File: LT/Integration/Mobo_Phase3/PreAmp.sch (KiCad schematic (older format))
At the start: 9 parts, among them J8 Conn_01x02_Male, J9 Conn_01x02_Female, Q2 Q_NJFET_DSG

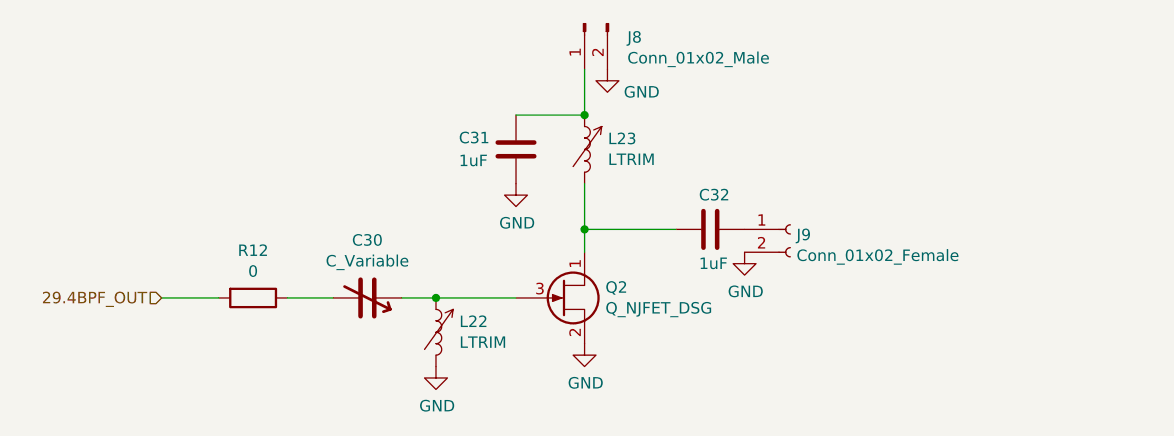
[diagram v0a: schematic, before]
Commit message: Finished PA Schematic Layout with footprints associated with it
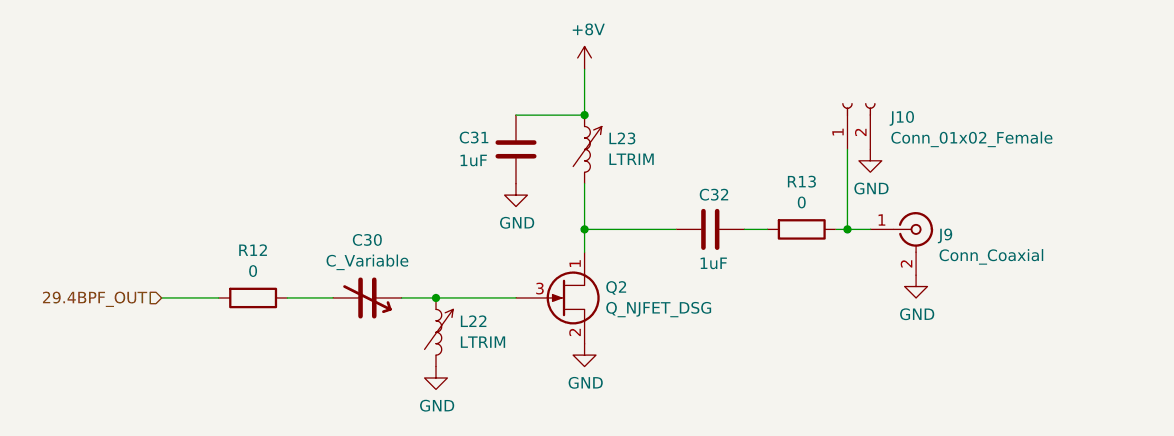
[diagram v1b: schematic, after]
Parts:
- removed J8: Conn_01x02_Male, Connector_PinHeader_2.54mm:PinHeader_1x02_P2.54mm_Vertical, symbol Connector:Conn_01x02_Male
- added J9: Conn_Coaxial, Connector_Coaxial:SMA_Amphenol_132291_Vertical, symbol Connector:Conn_Coaxial
- added R13: 0, Resistor_SMD:R_0805_2012Metric_Pad1.15x1.40mm_HandSolder, symbol Device:R
- renumbered J9 to J10
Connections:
- net GND: now also J9.2 (Ext)
- net +8V: now reaches C31.1, L23.1
- net at C32.1: now also R13.2; no longer J10.1 (Pin_1)
- new net: J10.1 (Pin_1), J9.1 (In), R13.1
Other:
- moved on the sheet: J10
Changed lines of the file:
@@
 	1    0    0    -1
-$EndComp
-$Comp
-L Connector:Conn_01x02_Male J8
-U 1 1 5EB64300
-P 4650 1950
-F 0 "J8" V 4710 1763 50  0000 R CNN
-F 1 "Conn_01x02_Male" V 4801 1763 50  0000 R CNN
-F 2 "Connector_PinHeader_2.54mm:PinHeader_1x02_P2.54mm_Vertical" H 4650 1950 50  0001 C CNN
-F 3 "~" H 4650 1950 50  0001 C CNN
-	1    4650 1950
-	0    -1   1    0
 $EndComp
 Wire Wire Line
 	4650 2150 4650 2350
 Connection ~ 4650 2350
-$Comp
-L power:GND #PWR0107
-U 1 1 5EB64481
-P 4750 2150
-F 0 "#PWR0107" H 4750 1900 50  0001 C CNN
-F 1 "GND" H 4900 2050 50  0000 C CNN
-F 2 "" H 4750 2150 50  0001 C CNN
-F 3 "" H 4750 2150 50  0001 C CNN
-	1    4750 2150
-	1    0    0    -1
-$EndComp
 $Comp
 L Daisy~Chain-cache:Device_C C32
@@
 	4650 2850 4650 2950
 $Comp
-L Connector:Conn_01x02_Female J9
+L Connector:Conn_01x02_Female J10
 U 1 1 5EB64662
-P 5550 2850
-F 0 "J9" H 5577 2826 50  0000 L CNN
-F 1 "Conn_01x02_Female" H 5577 2735 50  0000 L CNN
-F 2 "Connector_PinSocket_2.54mm:PinSocket_1x02_P2.54mm_Vertical" H 5550 2850 50  0001 C CNN
-F 3 "~" H 5550 2850 50  0001 C CNN
-	1    5550 2850
-	1    0    0    -1
+P 5800 2300
+F 0 "J10" V 5740 2112 50  0000 R CNN
+F 1 "Conn_01x02_Female" V 5649 2112 50  0000 R CNN
+F 2 "Connector_PinSocket_2.54mm:PinSocket_1x02_P2.54mm_Vertical" H 5800 2300 50  0001 C CNN
+F 3 "~" H 5800 2300 50  0001 C CNN
+	1    5800 2300
+	0    -1   -1   0
 $EndComp
 $Comp
 L power:GND #PWR0108
 U 1 1 5EB64C4A
-P 5350 2950
-F 0 "#PWR0108" H 5350 2700 50  0001 C CNN
-F 1 "GND" H 5355 2777 50  0000 C CNN
-F 2 "" H 5350 2950 50  0001 C CNN
-F 3 "" H 5350 2950 50  0001 C CNN
-	1    5350 2950
+P 5900 2500
+F 0 "#PWR0108" H 5900 2250 50  0001 C CNN
+F 1 "GND" H 5905 2327 50  0000 C CNN
+F 2 "" H 5900 2500 50  0001 C CNN
+F 3 "" H 5900 2500 50  0001 C CNN
+	1    5900 2500
 	1    0    0    -1
 $EndComp
+$Comp
+L Connector:Conn_Coaxial J9
+U 1 1 5EB6B925
+P 6100 2850
+F 0 "J9" H 6199 2826 50  0000 L CNN
+F 1 "Conn_Coaxial" H 6199 2735 50  0000 L CNN
+F 2 "Connector_Coaxial:SMA_Amphenol_132291_Vertical" H 6100 2850 50  0001 C CNN
+F 3 " ~" H 6100 2850 50  0001 C CNN
+	1    6100 2850
+	1    0    0    -1
+$EndComp
+$Comp
+L power:GND #PWR0109
+U 1 1 5EB6BA87
+P 6100 3050
+F 0 "#PWR0109" H 6100 2800 50  0001 C CNN
+F 1 "GND" H 6105 2877 50  0000 C CNN
+F 2 "" H 6100 3050 50  0001 C CNN
+F 3 "" H 6100 3050 50  0001 C CNN
+	1    6100 3050
+	1    0    0    -1
+$EndComp
+Wire Wire Line
+	5450 2850 5350 2850
+$Comp
+L Device:R R13
+U 1 1 5EB6C81C
+P 5600 2850
+F 0 "R13" V 5393 2850 50  0000 C CNN
+F 1 "0" V 5484 2850 50  0000 C CNN
+F 2 "Resistor_SMD:R_0805_2012Metric_Pad1.15x1.40mm_HandSolder" V 5530 2850 50  0001 C CNN
+F 3 "~" H 5600 2850 50  0001 C CNN
+	1    5600 2850
+	0    1    1    0
+$EndComp
+Wire Wire Line
+	5900 2850 5800 2850
+Wire Wire Line
+	5800 2500 5800 2850
+Connection ~ 5800 2850
+Wire Wire Line
+	5800 2850 5750 2850
+$Comp
+L power:+8V #PWR0107
+U 1 1 5EB725E6
+P 4650 2150
+F 0 "#PWR0107" H 4650 2000 50  0001 C CNN
+F 1 "+8V" H 4665 2323 50  0000 C CNN
+F 2 "" H 4650 2150 50  0001 C CNN
+F 3 "" H 4650 2150 50  0001 C CNN
+	1    4650 2150
+	1    0    0    -1
+$EndComp

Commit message: Changed 2pin headers to 5pin headers for output of pre-amp and input of PA
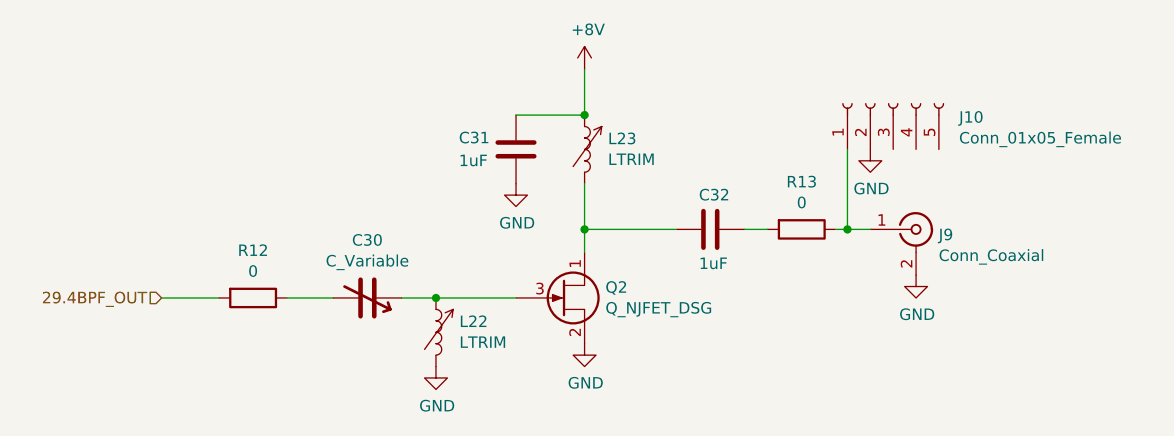
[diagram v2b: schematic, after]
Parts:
- removed J10: Conn_01x02_Female, Connector_PinSocket_2.54mm:PinSocket_1x02_P2.54mm_Vertical, symbol Connector:Conn_01x02_Female
- added J10: Conn_01x05_Female, Connector_PinSocket_2.54mm:PinSocket_1x05_P2.54mm_Vertical, symbol Connector:Conn_01x05_Female
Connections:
- net GND: now also J10.2 (Pin_2)
- net at J9.1 (In), R13.1: now also J10.1 (Pin_1)
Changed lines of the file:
@@
 	4650 2850 4650 2950
-$Comp
-L Connector:Conn_01x02_Female J10
-U 1 1 5EB64662
-P 5800 2300
-F 0 "J10" V 5740 2112 50  0000 R CNN
-F 1 "Conn_01x02_Female" V 5649 2112 50  0000 R CNN
-F 2 "Connector_PinSocket_2.54mm:PinSocket_1x02_P2.54mm_Vertical" H 5800 2300 50  0001 C CNN
-F 3 "~" H 5800 2300 50  0001 C CNN
-	1    5800 2300
-	0    -1   -1   0
-$EndComp
-$Comp
-L power:GND #PWR0108
-U 1 1 5EB64C4A
-P 5900 2500
-F 0 "#PWR0108" H 5900 2250 50  0001 C CNN
-F 1 "GND" H 5905 2327 50  0000 C CNN
-F 2 "" H 5900 2500 50  0001 C CNN
-F 3 "" H 5900 2500 50  0001 C CNN
-	1    5900 2500
-	1    0    0    -1
-$EndComp
 $Comp
 L Connector:Conn_Coaxial J9
@@
 	1    0    0    -1
 $EndComp
+$Comp
+L Connector:Conn_01x05_Female J10
+U 1 1 5EB9C6B4
+P 6000 2300
+F 0 "J10" V 5940 2012 50  0000 R CNN
+F 1 "Conn_01x05_Female" V 5849 2012 50  0000 R CNN
+F 2 "Connector_PinSocket_2.54mm:PinSocket_1x05_P2.54mm_Vertical" H 6000 2300 50  0001 C CNN
+F 3 "~" H 6000 2300 50  0001 C CNN
+	1    6000 2300
+	0    -1   -1   0
+$EndComp
+$Comp
+L power:GND #PWR0108
+U 1 1 5EB9E15B
+P 5900 2500
+F 0 "#PWR0108" H 5900 2250 50  0001 C CNN
+F 1 "GND" H 5905 2327 50  0000 C CNN
+F 2 "" H 5900 2500 50  0001 C CNN
+F 3 "" H 5900 2500 50  0001 C CNN
+	1    5900 2500
+	1    0    0    -1
+$EndComp

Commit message: Fixed the hierarchy for the MoBo Phase 3
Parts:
- C31, C32: symbol Daisy~Chain-cache:Device_C -> Mobo_Phase3-rescue:Device_C-Daisy_Chain-cache
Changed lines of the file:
@@
 EESchema Schematic File Version 4
-LIBS:Mobo_Phase3-cache
-EELAYER 26 0
+EELAYER 30 0
 EELAYER END
 $Descr A4 11693 8268
 encoding utf-8
-Sheet 6 8
+Sheet 5 8
 Title ""
 Date ""
@@
 $EndComp
 $Comp
-L Daisy~Chain-cache:Device_C C31
+L Mobo_Phase3-rescue:Device_C-Daisy_Chain-cache C31
 U 1 1 5EB62BDE
 P 4350 2500
@@
 Connection ~ 4650 2350
 $Comp
-L Daisy~Chain-cache:Device_C C32
+L Mobo_Phase3-rescue:Device_C-Daisy_Chain-cache C32
 U 1 1 5EB6449A
 P 5200 2850

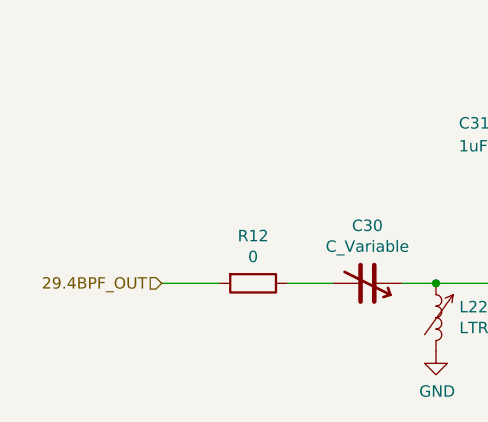
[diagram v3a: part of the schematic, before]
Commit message: Added the finalized layouts for the Mobo and Dobo Phase 3, as well as the preliminary layout for Phase 4 of both boards
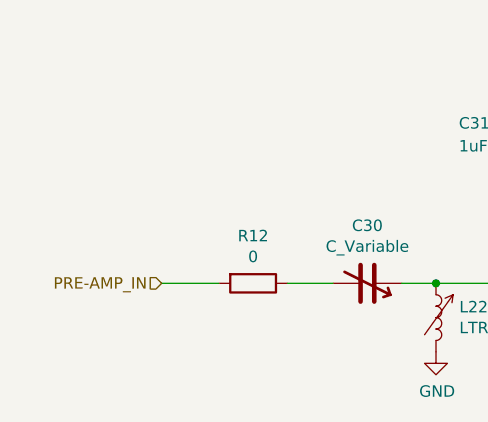
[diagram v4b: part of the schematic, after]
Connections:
- net 29.4BPF_OUT renamed PRE-AMP_IN
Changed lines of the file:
@@
 $EndComp
 Text HLabel 2800 3150 0    50   Input ~ 0
-29.4BPF_OUT
+PRE-AMP_IN
 Wire Wire Line
 	2800 3150 3050 3150
